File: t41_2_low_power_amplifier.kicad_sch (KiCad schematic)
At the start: 55 parts, among them J1 5-1814832-1, J2 5-1814832-1, J3 B2B-XH-A_LF__SN_, J5 Screw_Terminal_01x02, Q1 Q_NPN_BCE, Q10 Q_NPN_BEC, Q4 Q_NPN_BCE, Q7 Q_NPN_BEC, Q8 Q_NPN_BEC, Q9 Q_NPN_BEC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

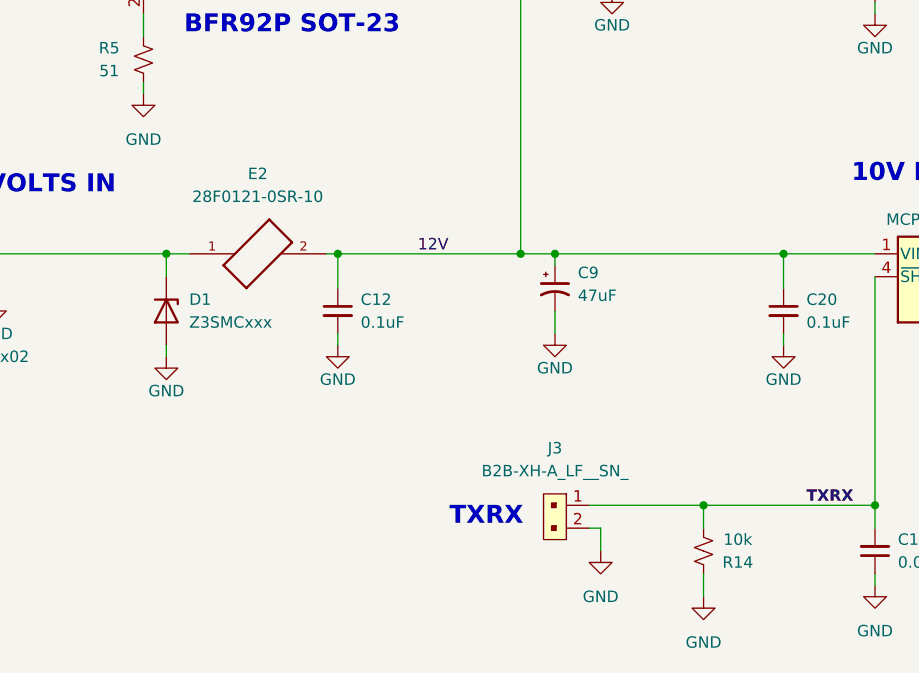
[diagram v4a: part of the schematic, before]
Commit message: Low Power Amplifier to fab.
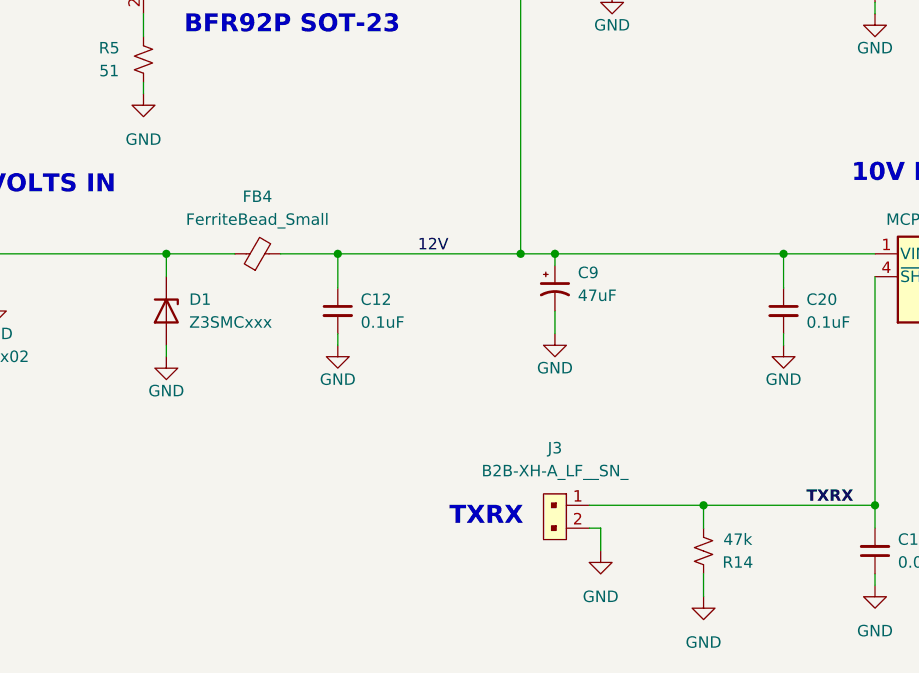
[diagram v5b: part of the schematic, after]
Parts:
- removed E2: 28F0121-0SR-10, 28F0121_0SR_10:FB_28F0121-0SR-10, symbol 28F0121-0SR-10:28F0121-0SR-10
- added FB4: FerriteBead_Small, Inductor_SMD:L_1206_3216Metric, symbol Device:FerriteBead_Small
- R14: value 10k -> 47k
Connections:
- net 12V: now also FB4.2
- net at D1.1 (K), J5.1 (Pin_1): now also FB4.1
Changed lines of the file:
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@@
 	(title_block
 		(title "T41-2 RF Power Amplifier")
-		(date "2024-12-19")
-		(rev "1.2")
+		(date "2025-01-19")
+		(rev "1.3")
 	)
 	(junction
@@
 	(wire
 		(pts
+			(xy 63.5 156.21) (xy 69.85 156.21)
+		)
+		(stroke
+			(width 0)
+			(type default)
+		)
+	)
+	(wire
+		(pts
 			(xy 130.81 73.66) (xy 133.35 73.66)
 		)
@@
 	(wire
 		(pts
-			(xy 68.58 156.21) (xy 69.85 156.21)
-		)
-		(stroke
-			(width 0)
-			(type default)
-		)
-	)
-	(wire
-		(pts
-			(xy 50.8 156.21) (xy 53.34 156.21)
+			(xy 50.8 156.21) (xy 58.42 156.21)
 		)
 		(stroke
@@
 	(label "10V_FIL"
 		(at 54.61 97.79 0)
-		(fields_autoplaced yes)
 		(effects
 			(font
@@
 	(label "10V_FIL"
 		(at 24.13 100.33 0)
-		(fields_autoplaced yes)
 		(effects
 			(font
@@
 	(label "BASE_BIAS"
 		(at 69.85 118.11 0)
-		(fields_autoplaced yes)
 		(effects
 			(font
@@
 	(label "10V_FIL"
 		(at 155.575 156.21 0)
-		(fields_autoplaced yes)
 		(effects
 			(font
@@
 	(label "10V_REG"
 		(at 176.53 156.21 0)
-		(fields_autoplaced yes)
 		(effects
 			(font
@@
 	(label "BASE_BIAS"
 		(at 115.57 68.58 0)
-		(fields_autoplaced yes)
 		(effects
 			(font
@@
 	(label "12V_REG"
 		(at 148.59 118.11 0)
-		(fields_autoplaced yes)
 		(effects
 			(font
@@
 	(label "12V_FINAL"
 		(at 176.53 68.58 0)
-		(fields_autoplaced yes)
 		(effects
 			(font
@@
 	(label "12V"
 		(at 78.74 156.21 0)
-		(fields_autoplaced yes)
 		(effects
 			(font
@@
 	(label "TXRX"
 		(at 121.92 184.15 0)
-		(fields_autoplaced yes)
 		(effects
 			(font
@@
 	(label "10V_REG"
 		(at 92.71 78.74 0)
-		(fields_autoplaced yes)
 		(effects
 			(font
@@
 	(label "12V_FINAL"
 		(at 175.26 118.11 0)
-		(fields_autoplaced yes)
 		(effects
 			(font
@@
 	(label "TXRX"
 		(at 107.95 127 0)
-		(fields_autoplaced yes)
 		(effects
 			(font
@@
 	)
 	(symbol
+		(lib_id "Device:FerriteBead_Small")
+		(at 60.96 156.21 90)
+		(unit 1)
+		(exclude_from_sim no)
+		(in_bom yes)
+		(on_board yes)
+		(dnp no)
+		(fields_autoplaced yes)
+		(property "Reference" "FB4"
+			(at 60.9219 149.86 90)
+			(effects
+				(font
+					(size 1.27 1.27)
+				)
+			)
+		)
+		(property "Value" "FerriteBead_Small"
+			(at 60.9219 152.4 90)
+			(effects
+				(font
+					(size 1.27 1.27)
+				)
+			)
+		)
+		(property "Footprint" "Inductor_SMD:L_1206_3216Metric"
+			(at 60.96 157.988 90)
+			(effects
+				(font
+					(size 1.27 1.27)
+				)
+				(hide yes)
+			)
+		)
+		(property "Datasheet" "~"
+			(at 60.96 156.21 0)
+			(effects
+				(font
+					(size 1.27 1.27)
+				)
+				(hide yes)
+			)
+		)
+		(property "Description" "Ferrite bead, small symbol"
+			(at 60.96 156.21 0)
+			(effects
+				(font
+					(size 1.27 1.27)
+				)
+				(hide yes)
+			)
+		)
+		(pin "1"
+		)
+		(pin "2"
+		)
+		(instances
+			(project "t41_2_low_power_amplifier"
+				(path "/2dfc3106-0fe9-4b2c-b32a-a54bf0a73e15"
+					(reference "FB4")
+					(unit 1)
+				)
+			)
+		)
+	)
+	(symbol
 		(lib_id "Device:R_Small_US")
 		(at 166.37 123.19 270)
@@
 			)
 		)
-		(property "Value" "10k"
+		(property "Value" "47k"
 			(at 114.3 187.96 0)
 			(effects
@@
 					(unit 1)
 				)
-			)
-		)
-	)
-	(symbol
-		(lib_id "28F0121-0SR-10:28F0121-0SR-10")
-		(at 60.96 156.21 0)
-		(unit 1)
-		(exclude_from_sim no)
-		(in_bom yes)
-		(on_board yes)
-		(dnp no)
-		(fields_autoplaced yes)
-		(property "Reference" "E2"
-			(at 60.96 147.32 0)
-			(effects
-				(font
-					(size 1.27 1.27)
-				)
-			)
-		)
-		(property "Value" "28F0121-0SR-10"
-			(at 60.96 149.86 0)
-			(effects
-				(font
-					(size 1.27 1.27)
-				)
-			)
-		)
-		(property "Footprint" "28F0121_0SR_10:FB_28F0121-0SR-10"
-			(at 60.96 156.21 0)
-			(effects
-				(font
-					(size 1.27 1.27)
-				)
-				(justify bottom)
-				(hide yes)
-			)
-		)
-		(property "Datasheet" ""
-			(at 60.96 156.21 0)
-			(effects
-				(font
-					(size 1.27 1.27)
-				)
-				(hide yes)
-			)
-		)
-		(property "Description" ""
-			(at 60.96 156.21 0)
-			(effects
-				(font
-					(size 1.27 1.27)
-				)
-				(hide yes)
-			)
-		)
-		(property "PARTREV" "J"
-			(at 60.96 156.21 0)
-			(effects
-				(font
-					(size 1.27 1.27)
-				)
-				(justify bottom)
-				(hide yes)
-			)
-		)
-		(property "STANDARD" "Manufacturer Recommendations"
-			(at 60.96 156.21 0)
-			(effects
-				(font
-					(size 1.27 1.27)
-				)
-				(justify bottom)
-				(hide yes)
-			)
-		)
-		(property "MAXIMUM_PACKAGE_HEIGHT" "3.05 mm"
-			(at 60.96 156.21 0)
-			(effects
-				(font
-					(size 1.27 1.27)
-				)
-				(justify bottom)
-				(hide yes)
-			)
-		)
-		(property "MANUFACTURER" "Laird"
-			(at 60.96 156.21 0)
-			(effects
-				(font
-					(size 1.27 1.27)
-				)
-				(justify bottom)
-				(hide yes)
-			)
-		)
-		(pin "2"
-		)
-		(pin "1"
-		)
-		(instances
-			(project "t41_2_power_amplifier"
-				(path "/2dfc3106-0fe9-4b2c-b32a-a54bf0a73e15"
-					(reference "E2")
-					(unit 1)
-				)

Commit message: Release to fab.
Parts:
- added R27: 10, Resistor_SMD:R_1206_3216Metric, symbol Device:R_Small_US
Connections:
- net 12V: now also R27.1; no longer FB2.1
- new net: FB2.1, R27.2
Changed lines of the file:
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@@
 (kicad_sch
-	(version 20231120)
+	(version 20250114)
 	(generator "eeschema")
-	(generator_version "8.0")
+	(generator_version "9.0")
 	(paper "USLetter")
 	(title_block
@@
 		(rev "1.3")
 	)
+	(text "OUTPUT"
+		(exclude_from_sim no)
+		(at 222.25 53.34 0)
+		(effects
+			(font
+				(size 2 2)
+				(thickness 0.4)
+				(bold yes)
+			)
+		)
+	)
+	(text "PUSH-PULL OUTPUT STAGE"
+		(exclude_from_sim no)
+		(at 151.13 33.02 0)
+		(effects
+			(font
+				(size 2 2)
+				(thickness 0.4)
+				(bold yes)
+			)
+		)
+	)
+	(text "BFU590G SOT-223"
+		(exclude_from_sim no)
+		(at 179.07 45.72 0)
+		(effects
+			(font
+				(size 2 2)
+				(thickness 0.4)
+				(bold yes)
+			)
+		)
+	)
+	(text "BIASING CIRCUIT"
+		(exclude_from_sim no)
+		(at 45.72 92.71 0)
+		(effects
+			(font
+				(size 2 2)
+				(thickness 0.4)
+				(bold yes)
+			)
+		)
+	)
+	(text "SOT-23 MMBT5551LT1G"
+		(exclude_from_sim no)
+		(at 78.74 101.6 0)
+		(effects
+			(font
+				(size 2 2)
+				(thickness 0.4)
+				(bold yes)
+			)
+		)
+	)
+	(text "+13.4 VOLTS IN"
+		(exclude_from_sim no)
+		(at 33.02 148.59 0)
+		(effects
+			(font
+				(size 2 2)
+				(thickness 0.4)
+				(bold yes)
+			)
+		)
+	)
+	(text "TXRX"
+		(exclude_from_sim no)
+		(at 86.36 185.42 0)
+		(effects
+			(font
+				(size 2 2)
+				(thickness 0.4)
+				(bold yes)
+			)
+		)
+	)
+	(text "T41-2 RF LOW POWER AMPLIFIER"
+		(exclude_from_sim no)
+		(at 129.54 19.05 0)
+		(effects
+			(font
+				(size 3 3)
+				(thickness 0.6)
+				(bold yes)
+			)
+		)
+	)
+	(text "BFR106 SOT-23"
+		(exclude_from_sim no)
+		(at 66.04 46.99 0)
+		(effects
+			(font
+				(size 2 2)
+				(thickness 0.4)
+				(bold yes)
+			)
+		)
+	)
+	(text "INPUT"
+		(exclude_from_sim no)
+		(at 21.59 52.07 0)
+		(effects
+			(font
+				(size 2 2)
+				(thickness 0.4)
+				(bold yes)
+			)
+		)
+	)
+	(text "10V REGULATOR"
+		(exclude_from_sim no)
+		(at 139.7 147.32 0)
+		(effects
+			(font
+				(size 2 2)
+				(thickness 0.4)
+				(bold yes)
+			)
+		)
+	)
+	(text "WIDEBAND DARLINGTON AMPLIFIER"
+		(exclude_from_sim no)
+		(at 68.58 43.18 0)
+		(effects
+			(font
+				(size 2 2)
+				(thickness 0.4)
+				(bold yes)
+			)
+		)
+	)
+	(text "BFR92P SOT-23"
+		(exclude_from_sim no)
+		(at 64.77 130.81 0)
+		(effects
+			(font
+				(size 2 2)
+				(thickness 0.4)
+				(bold yes)
+			)
+		)
+	)
+	(text "12V REGULATOR"
+		(exclude_from_sim no)
+		(at 130.81 107.95 0)
+		(effects
+			(font
+				(size 2 2)
+				(thickness 0.4)
+				(bold yes)
+			)
+		)
+	)
 	(junction
 		(at 69.85 156.21)
@@
 	(wire
 		(pts
+			(xy 90.17 156.21) (xy 93.98 156.21)
+		)
+		(stroke
+			(width 0)
+			(type default)
+		)
+	)
+	(wire
+		(pts
 			(xy 243.84 146.05) (xy 243.84 148.59)
 		)
@@
 	(wire
 		(pts
-			(xy 90.17 118.11) (xy 90.17 156.21)
-		)
-		(stroke
-			(width 0)
-			(type default)
-		)
-	)
-	(wire
-		(pts
 			(xy 156.21 95.25) (xy 156.21 96.52)
 		)
@@
 	(wire
 		(pts
+			(xy 90.17 138.43) (xy 90.17 156.21)
+		)
+		(stroke
+			(width 0)
+			(type default)
+		)
+	)
+	(wire
+		(pts
 			(xy 125.73 73.66) (xy 123.19 73.66)
 		)
@@
 	(wire
 		(pts
+			(xy 90.17 118.11) (xy 90.17 133.35)
+		)
+		(stroke
+			(width 0)
+			(type default)
+		)
+	)
+	(wire
+		(pts
 			(xy 152.4 156.21) (xy 165.1 156.21)
 		)
@@
 	(wire
 		(pts
-			(xy 90.17 156.21) (xy 93.98 156.21)
-		)
-		(stroke
-			(width 0)
-			(type default)
-		)
-	)
-	(wire
-		(pts
 			(xy 110.49 191.77) (xy 110.49 194.31)
 		)
@@
 		)
 	)
-	(text "OUTPUT"
-		(exclude_from_sim no)
-		(at 222.25 53.34 0)
-		(effects
-			(font
-				(size 2 2)
-				(thickness 0.4)
-				(bold yes)
-			)
-		)
-	)
-	(text "PUSH-PULL OUTPUT STAGE"
-		(exclude_from_sim no)
-		(at 151.13 33.02 0)
-		(effects
-			(font
-				(size 2 2)
-				(thickness 0.4)
-				(bold yes)
-			)
-		)
-	)
-	(text "BFU590G SOT-223"
-		(exclude_from_sim no)
-		(at 179.07 45.72 0)
-		(effects
-			(font
-				(size 2 2)
-				(thickness 0.4)
-				(bold yes)
-			)
-		)
-	)
-	(text "BIASING CIRCUIT"
-		(exclude_from_sim no)
-		(at 45.72 92.71 0)
-		(effects
-			(font
-				(size 2 2)
-				(thickness 0.4)
-				(bold yes)
-			)
-		)
-	)
-	(text "SOT-23 MMBT5551LT1G"
-		(exclude_from_sim no)
-		(at 78.74 101.6 0)
-		(effects
-			(font
-				(size 2 2)
-				(thickness 0.4)
-				(bold yes)
-			)
-		)
-	)
-	(text "+13.4 VOLTS IN"
-		(exclude_from_sim no)
-		(at 33.02 148.59 0)
-		(effects
-			(font
-				(size 2 2)
-				(thickness 0.4)
-				(bold yes)
-			)
-		)
-	)
-	(text "TXRX"
-		(exclude_from_sim no)
-		(at 86.36 185.42 0)
-		(effects
-			(font
-				(size 2 2)
-				(thickness 0.4)
-				(bold yes)
-			)
-		)
-	)
-	(text "T41-2 RF LOW POWER AMPLIFIER"
-		(exclude_from_sim no)
-		(at 129.54 19.05 0)
-		(effects
-			(font
-				(size 3 3)
-				(thickness 0.6)
-				(bold yes)
-			)
-		)
-	)
-	(text "BFR106 SOT-23"
-		(exclude_from_sim no)
-		(at 66.04 46.99 0)
-		(effects
-			(font
-				(size 2 2)
-				(thickness 0.4)
-				(bold yes)
-			)
-		)
-	)
-	(text "INPUT"
-		(exclude_from_sim no)
-		(at 21.59 52.07 0)
-		(effects
-			(font
-				(size 2 2)
-				(thickness 0.4)
-				(bold yes)
-			)
-		)
-	)
-	(text "10V REGULATOR"
-		(exclude_from_sim no)
-		(at 139.7 147.32 0)
-		(effects
-			(font
-				(size 2 2)
-				(thickness 0.4)
-				(bold yes)
-			)
-		)
-	)
-	(text "WIDEBAND DARLINGTON AMPLIFIER"
-		(exclude_from_sim no)
-		(at 68.58 43.18 0)
-		(effects
-			(font
-				(size 2 2)
-				(thickness 0.4)
-				(bold yes)
-			)
-		)
-	)
-	(text "BFR92P SOT-23"
-		(exclude_from_sim no)
-		(at 64.77 130.81 0)
-		(effects
-			(font
-				(size 2 2)
-				(thickness 0.4)
-				(bold yes)
-			)
-		)
-	)
-	(text "12V REGULATOR"
-		(exclude_from_sim no)
-		(at 130.81 107.95 0)
-		(effects
-			(font
-				(size 2 2)
-				(thickness 0.4)
-				(bold yes)
-			)
-		)
-	)
 	(label "10V_FIL"
 		(at 54.61 97.79 0)
@@
 	)
 	(symbol
+		(lib_id "Device:R_Small_US")
+		(at 90.17 135.89 180)
+		(unit 1)
+		(exclude_from_sim no)
+		(in_bom yes)
+		(on_board yes)
+		(dnp no)
+		(property "Reference" "R27"
+			(at 87.63 134.62 0)
+			(effects
+				(font
+					(size 1.27 1.27)
+				)
+			)
+		)
+		(property "Value" "10"
+			(at 87.63 137.16 0)
+			(do_not_autoplace yes)
+			(effects
+				(font
+					(size 1.27 1.27)
+				)
+			)
+		)
+		(property "Footprint" "Resistor_SMD:R_1206_3216Metric"
+			(at 90.17 135.89 0)
+			(effects
+				(font
+					(size 1.27 1.27)
+				)
+				(hide yes)
+			)
+		)
+		(property "Datasheet" "~"
+			(at 90.17 135.89 0)
+			(effects
+				(font
+					(size 1.27 1.27)
+				)
+				(hide yes)
+			)
+		)
+		(property "Description" "Resistor, small US symbol"
+			(at 90.17 135.89 0)
+			(effects
+				(font
+					(size 1.27 1.27)
+				)
+				(hide yes)
+			)
+		)
+		(pin "2"
+		)
+		(pin "1"
+		)
+		(instances
+			(project "t41_2_low_power_amplifier"
+				(path "/2dfc3106-0fe9-4b2c-b32a-a54bf0a73e15"
+					(reference "R27")
+					(unit 1)
+				)
+			)
+		)
+	)
+	(symbol
 		(lib_id "power:GND")
 		(at 220.98 69.85 0)
@@
 		)
 	)
+	(embedded_fonts no)
 )

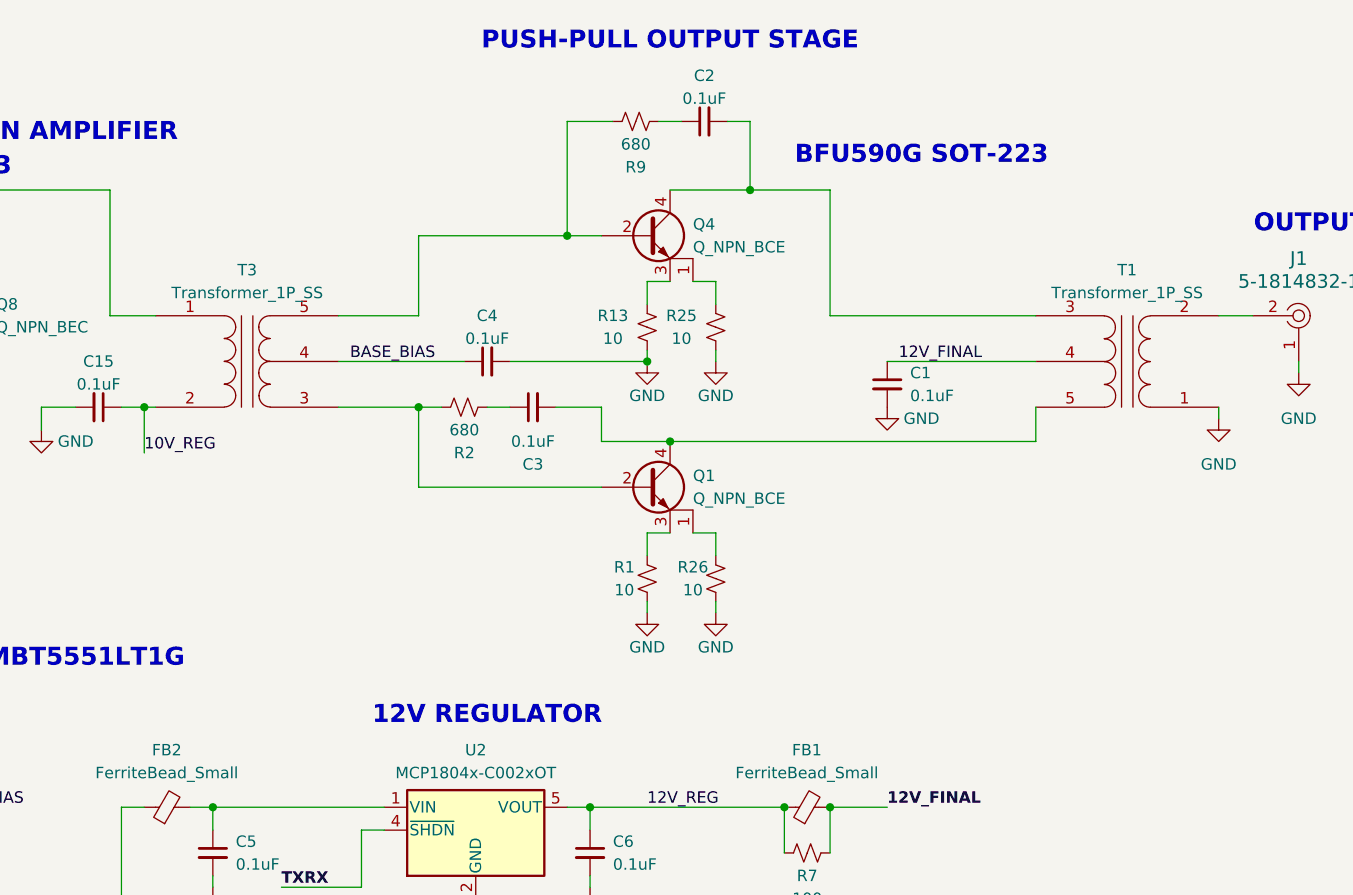
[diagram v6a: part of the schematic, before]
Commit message: Updated notes on schematic.
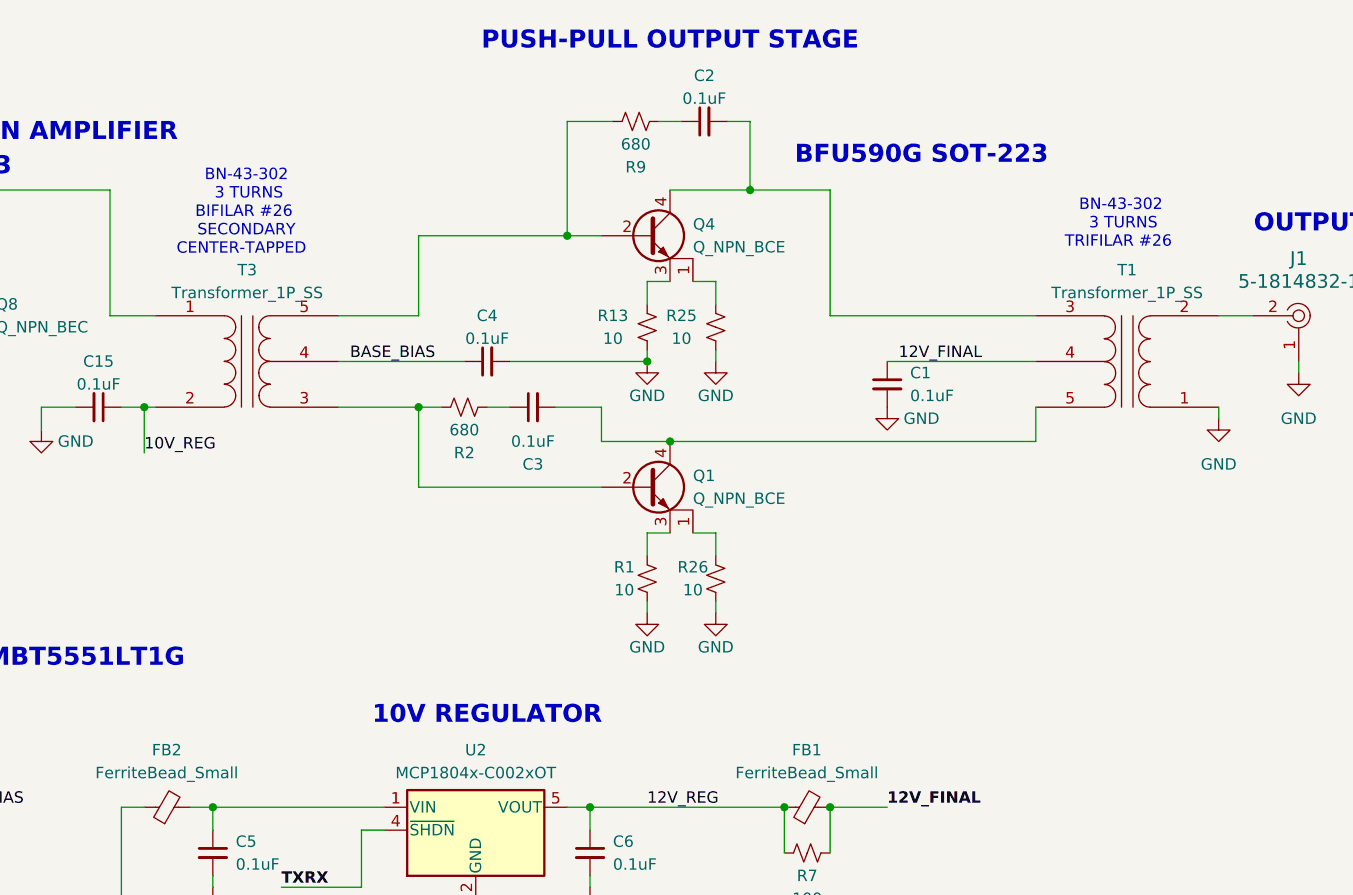
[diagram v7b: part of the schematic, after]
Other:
- note added: "BN-43-302 3 TURNS BIFILAR #26 SECONDARY CENTER-TAPPED"
- note added: "BN-43-302 3 TURNS TRIFILAR #26"
- note removed: "12V REGULATOR"
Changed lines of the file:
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@@
+		)
+	)
+	(text "  BN-43-302\n   3 TURNS\n TRIFILAR #26"
+		(exclude_from_sim no)
+		(at 200.66 53.34 0)
+		(effects
+			(font
+				(size 1.27 1.27)
+			)
 		)
 	)
@@
 		)
 	)
+	(text "  BN-43-302\n   3 TURNS\n BIFILAR #26\n  SECONDARY\nCENTER-TAPPED"
+		(exclude_from_sim no)
+		(at 103.505 52.07 0)
+		(effects
+			(font
+				(size 1.27 1.27)
+			)
+		)
+	)
 	(text "WIDEBAND DARLINGTON AMPLIFIER"
 		(exclude_from_sim no)
@@
 		)
 	)
-	(text "12V REGULATOR"
+	(text "10V REGULATOR"
 		(exclude_from_sim no)
 		(at 130.81 107.95 0)

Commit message: Updated schematic notes.
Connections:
- net 12V_FINAL renamed 10V_FINAL_REG
- net 12V_REG: no longer names the net of C6.1, FB1.1, R7.2, U2.5 (VOUT)
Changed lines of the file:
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@@
 		)
 	)
-	(label "12V_REG"
-		(at 148.59 118.11 0)
-		(effects
-			(font
-				(size 1.27 1.27)
-			)
-			(justify left bottom)
-		)
-	)
-	(label "12V_FINAL"
+	(label "10V_FINAL_REG"
 		(at 176.53 68.58 0)
 		(effects
@@
 		)
 	)
-	(label "12V_FINAL"
+	(label "10V_FINAL_REG"
 		(at 175.26 118.11 0)
 		(effects
